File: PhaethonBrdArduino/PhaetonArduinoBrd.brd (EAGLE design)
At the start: 68.6 x 53.3 mm, 40 parts, among them IC1 DS1307, IC2 LM2596S, Q1 32.768 Hz, SW1 EC12E_SW

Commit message: i hope final layout before seed studio
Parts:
- moved RESET 0.76 mm to (6.22, 49.1)
- moved C_OUTPUT 0.54 mm to (19.7, 7.75)
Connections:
- new net PIN11: J3.4, J4.4
- new net PIN12: J3.5, J4.5
- new net PIN13: J3.6, J4.6
- new net SCLK: U$2.4
- net MISO: no longer J3.5, J4.5
- net MOSI: no longer J3.4, J4.4
- net SCK: no longer J3.6, J4.6, U$2.4
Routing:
- net +5V: track 47.8 -> 143.3 mm, vias 1 -> 4
- net PIN6: track 2.54 -> 55.5 mm
- net PIN2: track 2.63 -> 50.7 mm
- net A0: track 43.4 -> 68.7 mm, vias 1 -> 2
- net GND: track 221.2 -> 241.0 mm, vias 2 -> 4
- net SCL: track 34.7 -> 51.4 mm
- net MOSI: track 2.54 -> 16.4 mm
- net PIN5: track 2.54 -> 14.0 mm
- net PIN3: track 38.9 -> 49.4 mm, vias 1 -> 0
- net SDA: track 29.3 -> 39.6 mm, vias 2 -> 0
- net MISO: track 2.54 -> 12.1 mm
- net OUTPUT1: track 20.1 -> 27.8 mm
- net PIN4: track 40.9 -> 34.0 mm, vias 2 -> 0
- net OUTPUT5V: track 42.5 -> 36.0 mm
- net +24V: track 45.2 -> 50.9 mm, vias 3 -> 2
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
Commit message: a lot of bug fixes
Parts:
- LED: value GM5WA94310A -> (none)
- moved C_OUTPUT 0.54 mm to (19.3, 7.37)
- moved L1 0.46 mm to (8.00, 7.50), turned to 0 degrees
- moved RESET 0.26 mm to (6.22, 49.4)
- renumbered IC1 to DS1307, LED1 to LED, SL1 to DISPLAYCONNECTOR, U$2 to ADT
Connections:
- removed net N$141: J3.9, J4.9
- removed net N$142: J3.10, J4.10
- removed net N$23: ANALOG.6, J6.6
- removed net PIN11: J3.4, J4.4
- removed net PIN12: J3.5, J4.5
- removed net PIN13: J3.6, J4.6
- removed net SCLK: ADT.4
- new net A3: ANALOG.4, J6.4
- net MISO: now also J3.5, J4.5
- net MOSI: now also J3.4, J4.4
- net OUTPUT1: now also L1.P$1; no longer L1.P$2
- net OUTPUT5V: now also L1.P$2; no longer L1.P$1
- net SCK: now also ADT.4, J3.6, J4.6
- net SCL: now also ANALOG.6, J3.10, J4.10, J6.6; no longer ANALOG.5, J6.5
- net SDA: now also ANALOG.5, J3.9, J4.9, J6.5; no longer ANALOG.4, J6.4
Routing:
- net SCK: track 0.00 -> 91.9 mm, vias 0 -> 2
- net SCL: track 51.4 -> 101.0 mm, vias 0 -> 1
- net MISO: track 12.1 -> 60.7 mm, vias 0 -> 1
- net MOSI: track 16.4 -> 56.5 mm, vias 0 -> 3
- net SDA: track 39.6 -> 76.0 mm
- net GND: track 241.0 -> 277.4 mm, vias 4 -> 0
- net A0: track 68.7 -> 43.4 mm, vias 2 -> 3
- net A1: track 52.9 -> 71.0 mm
- net +5V: track 143.3 -> 126.7 mm, vias 4 -> 2
- net OUTPUT1: track 27.8 -> 16.9 mm
- net PIN3: track 49.4 -> 38.8 mm
- net PIN2: track 50.7 -> 40.2 mm
- net RESET: track 116.8 -> 124.9 mm, vias 5 -> 7
- net OUTPUT5V: track 36.0 -> 40.8 mm
- net PIN6: track 55.5 -> 52.4 mm
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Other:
- board text added: "Phaethon"
- board text removed: "REV3"

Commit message: Issue: Change the RGB LED #1
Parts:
- added R12: 230, SparkFun:0805
- added R13: 90, SparkFun:0805
- LED: value (none) -> WL-SFTW-150141M173100-R&G&B; device led:GM5WA94310A -> Wuerth_Elektronik_LEDs_rev15b:3528-COMMON-ANODE
- R11: value 10K\ -> 125
- moved R11 3.83 mm to (35.7, 42.3), turned to 270 degrees
- moved LED 1.02 mm to (43.9, 42.2), turned to 180 degrees
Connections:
- removed net N$11: LED.4, LED.5, LED.6, R11.2
- new net N$1: LED.2, R11.1
- new net N$2: LED.3, R12.1
- new net N$3: LED.4, R13.1
- net +5V: now also LED.1
- net A0: now also R11.2; no longer LED.1
- net A1: now also R13.2; no longer LED.2
- net A2: now also R12.2; no longer LED.3
- net GND: no longer R11.1
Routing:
- net A1: track 71.0 -> 45.3 mm, vias 2 -> 3
- net A2: track 49.1 -> 71.4 mm, vias 3 -> 1
- net N$2: track 0.00 -> 17.3 mm
- net SCK: track 91.9 -> 75.1 mm, vias 2 -> 3
- net +5V: track 126.7 -> 141.5 mm, vias 2 -> 3
- net GND: track 277.4 -> 265.6 mm
- net N$3: track 0.00 -> 11.1 mm
- net N$1: track 0.00 -> 7.63 mm
- net A0: track 43.4 -> 48.5 mm, vias 3 -> 1
- net N$11: track 4.23 -> 0.00 mm

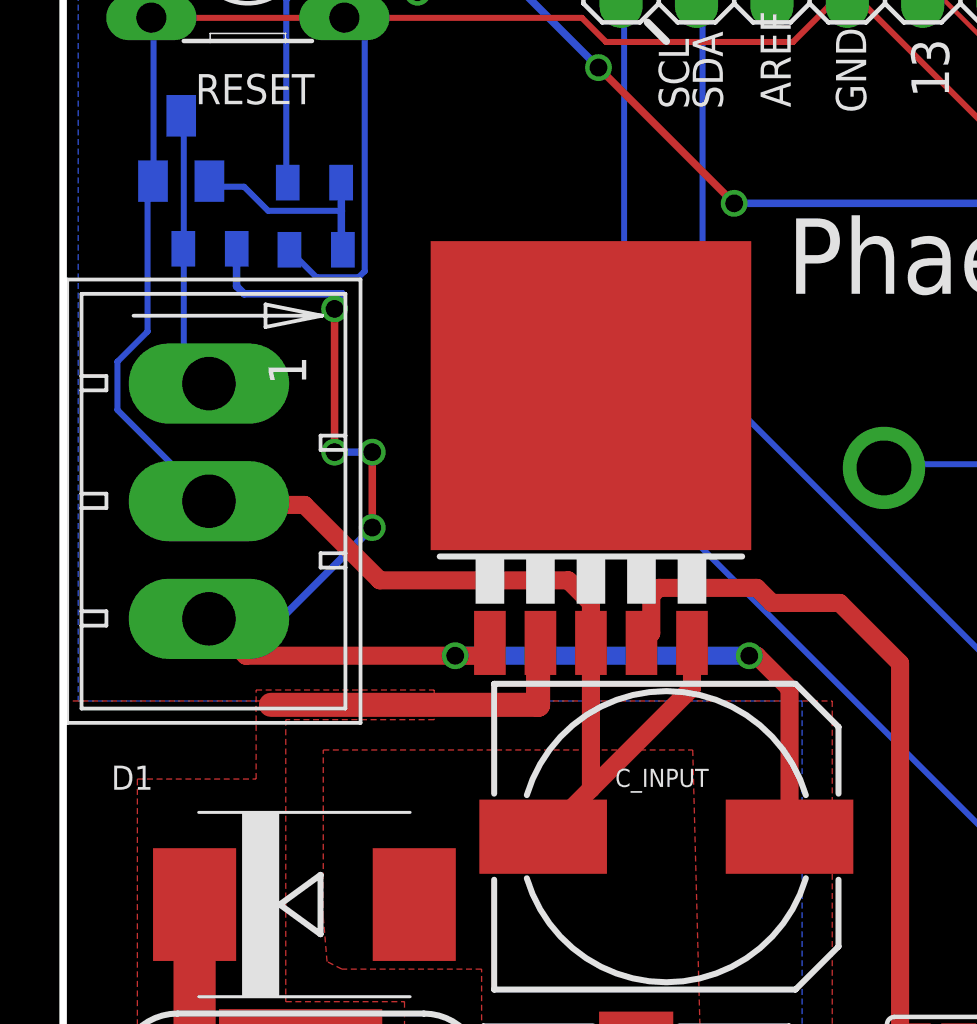
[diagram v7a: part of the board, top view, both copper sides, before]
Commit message: Added bridge, Issue #3
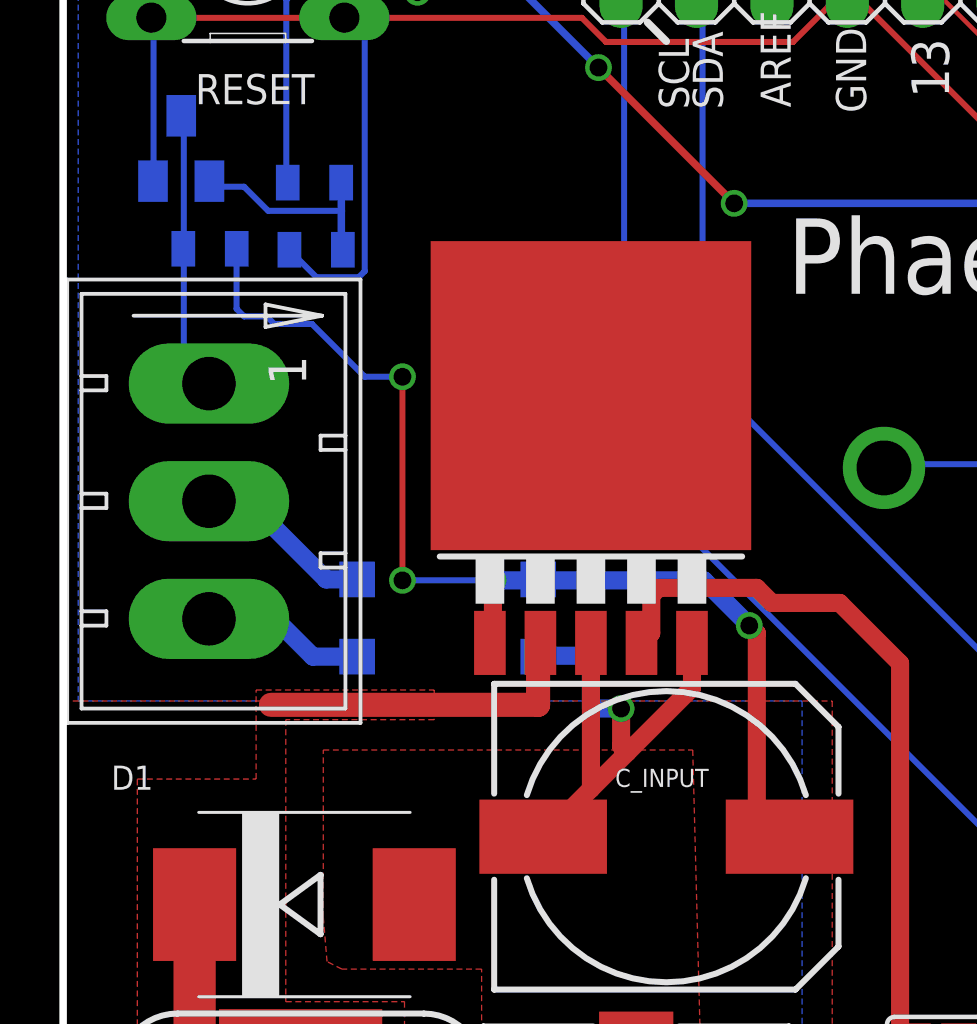
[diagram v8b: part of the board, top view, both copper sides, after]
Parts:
- added B1: MB2S, rectifier:SOIC-4
- R13: value 90 -> 768
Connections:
- new net N$4: B1.~1, SV1.3
- new net N$6: B1.~2, SV1.2
- net +24V: now also B1.+; no longer SV1.3
- net GND: now also B1.-; no longer SV1.2
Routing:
- net GND: track 265.6 -> 243.5 mm, vias 0 -> 1
- net +24V: track 48.3 -> 38.5 mm, vias 6 -> 4
- net N$6: track 0.00 -> 6.08 mm
- net N$4: track 0.00 -> 5.54 mm
